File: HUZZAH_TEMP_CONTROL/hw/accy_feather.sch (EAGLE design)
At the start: 7 parts

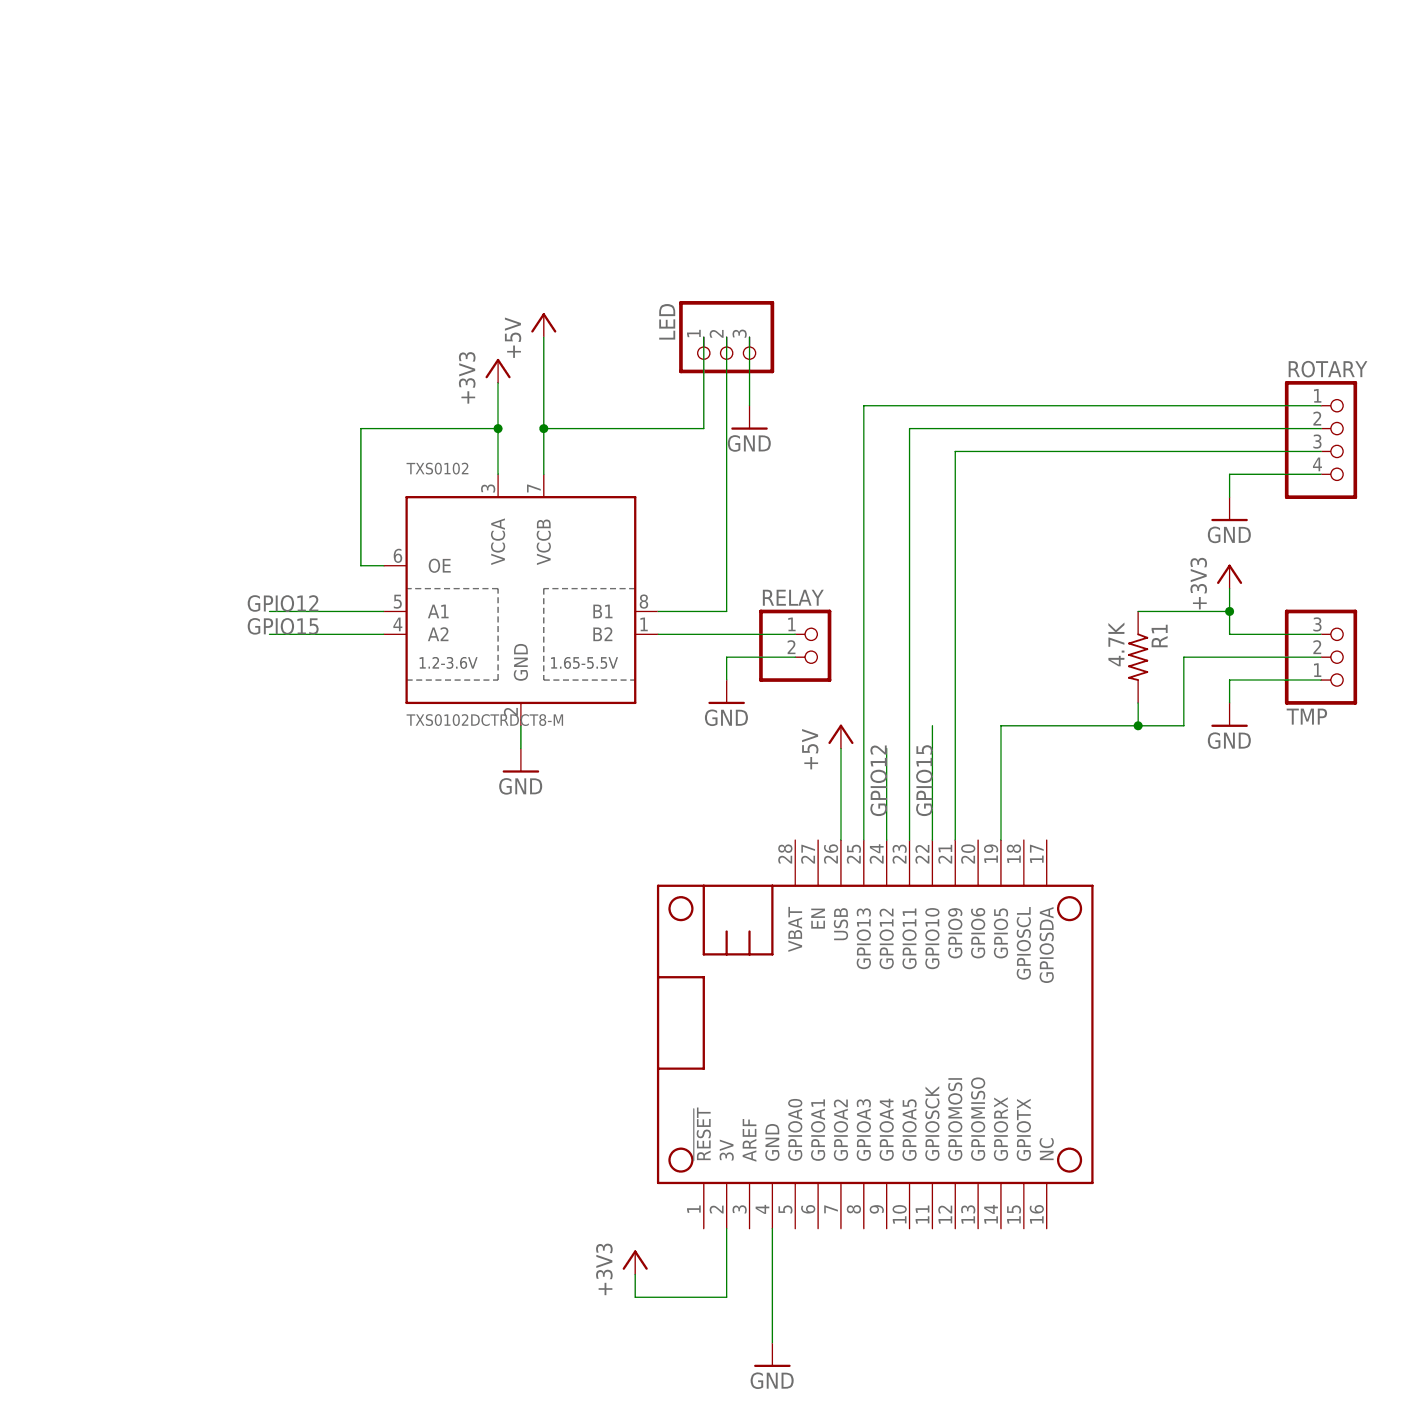
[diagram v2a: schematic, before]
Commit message: Accessory board version 2.0
Added a pulldown on the high voltage side of the relay output.  This
is needed because the level shifter can drive it high when it's floating
which causes board instability.

Added on-board 10A relay (Digi-Key Part #Z2763-ND) to the bottom side.
There are 2 choices for relay control now:
  - You can place the "Relay Drive" header and wire an external relay
    or SSR.  This is a good choice for high current loads like compressors.
                                   or
  - You can place the 10 relay Digi-Key Part #Z2763-ND) and the
    "Relay Switch" header.  The externally switched power can be run
    through the "Relay Switch" header.  This is good for lower current
    resistive heaters.
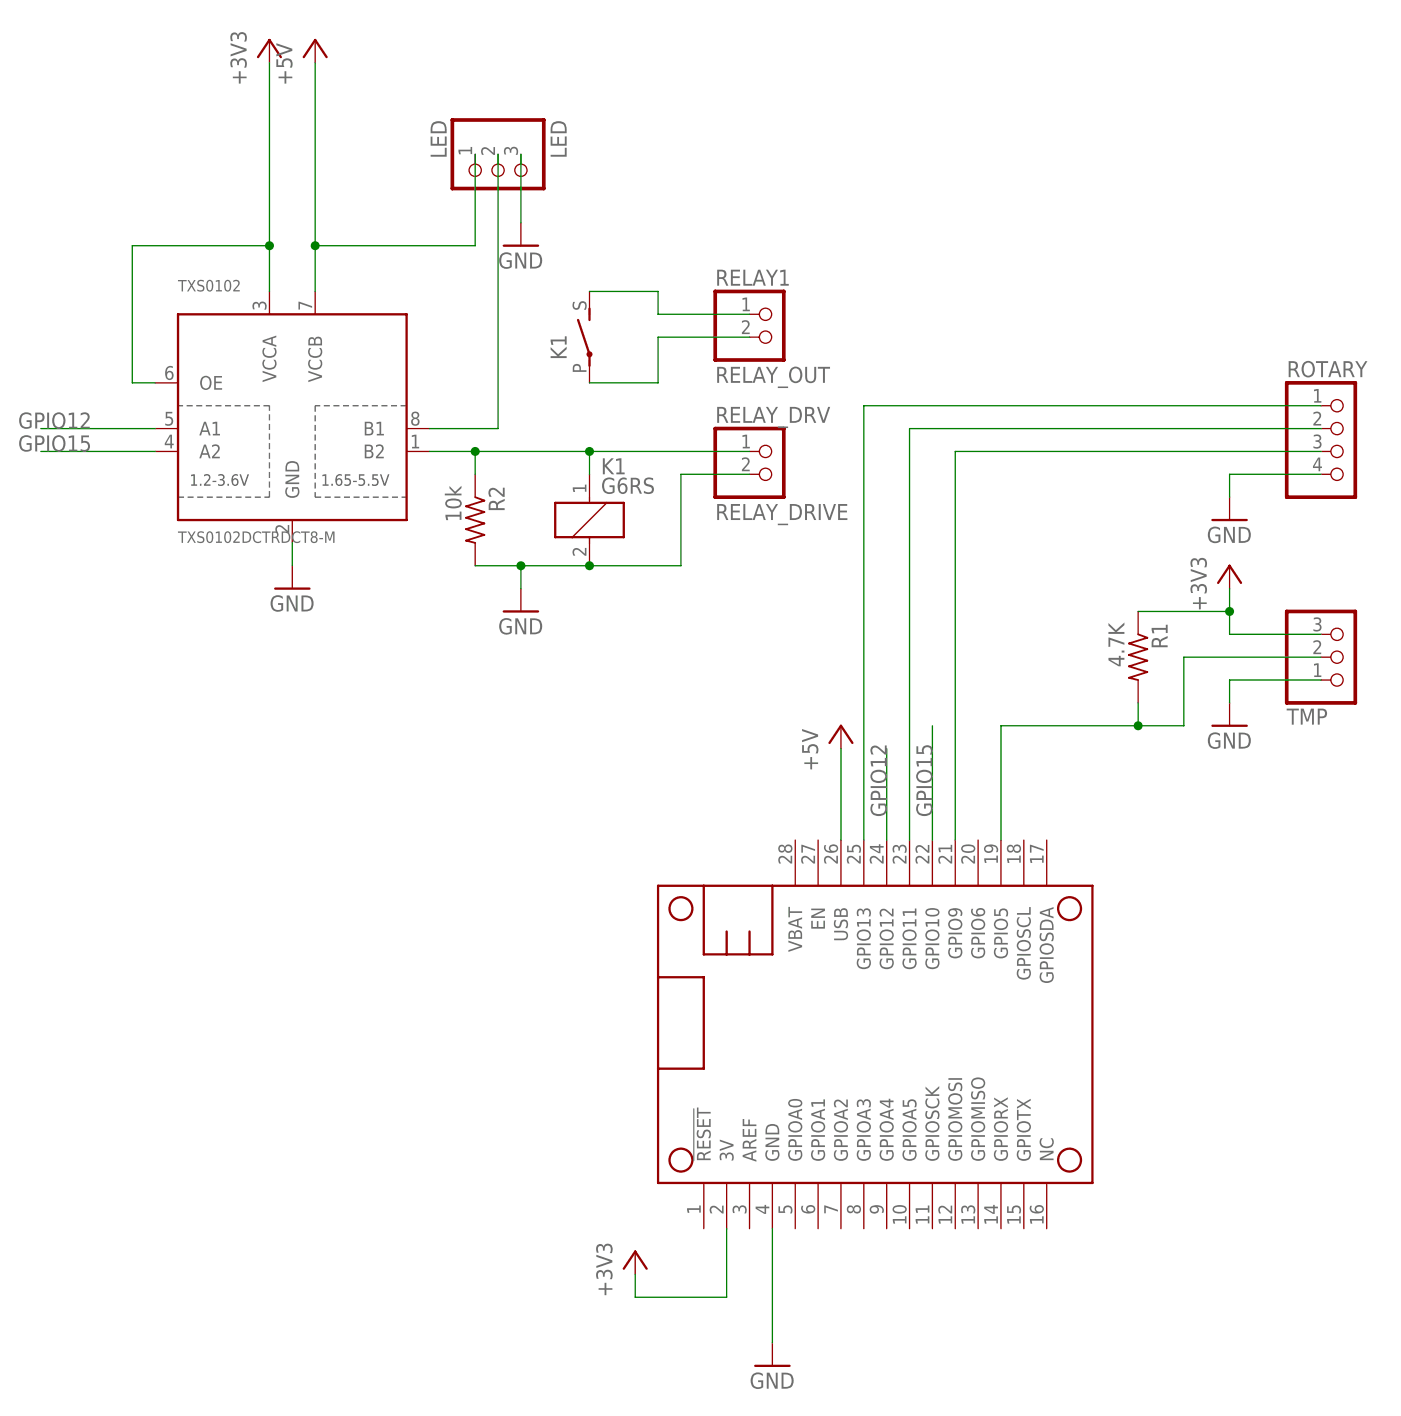
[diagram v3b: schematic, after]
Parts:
- removed RELAY: (no value), pinhead:PINHD-1X2
- added K1: G6RS, relay:G6RS
- added R2: 10k, resistor:R-US_R0603
- added RELAY1: RELAY_OUT, pinhead:PINHD-1X2
- added RELAY_DRV: RELAY_DRIVE, pinhead:PINHD-1X2
- LED: value (none) -> LED
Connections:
- new net N$2: K12.P, RELAY1.2
- new net RELAY_CTRL: K12.S, RELAY1.1
- net GND: now also K11.2, R2.2, RELAY_DRV.2; no longer RELAY.2
- net RELAY: now also K11.1, R2.1, RELAY_DRV.1; no longer RELAY.1
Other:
- moved on the sheet: LED, TXS0102
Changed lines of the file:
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@@
 <part name="GND5" library="supply1" deviceset="GND" device=""/>
 <part name="TMP" library="adafruit" deviceset="PINHD-1X3" device="CB"/>
-<part name="LED" library="adafruit" deviceset="PINHD-1X3" device="CB"/>
+<part name="LED" library="adafruit" deviceset="PINHD-1X3" device="CB" value="LED"/>
 <part name="GND6" library="supply1" deviceset="GND" device=""/>
 <part name="GND3" library="supply1" deviceset="GND" device=""/>
-<part name="RELAY" library="pinhead" deviceset="PINHD-1X2" device=""/>
+<part name="RELAY_DRV" library="pinhead" deviceset="PINHD-1X2" device="" value="RELAY_DRIVE"/>
 <part name="ROTARY" library="pinhead" deviceset="PINHD-1X4" device=""/>
 <part name="TXS0102" library="DZ" deviceset="TXS0102DCTR" device="DCT8-M"/>
+<part name="R2" library="resistor" deviceset="R-US_" device="R0603" value="10k"/>
+<part name="K1" library="relay" deviceset="G6RS" device=""/>
+<part name="RELAY1" library="pinhead" deviceset="PINHD-1X2" device="" value="RELAY_OUT"/>
 </parts>
 <sheets>
@@
 <instance part="P+1" gate="1" x="96.52" y="96.52"/>
 <instance part="+3V2" gate="G$1" x="139.7" y="114.3"/>
-<instance part="P+2" gate="1" x="63.5" y="142.24"/>
-<instance part="GND4" gate="1" x="60.96" y="91.44"/>
+<instance part="P+2" gate="1" x="38.1" y="172.72"/>
+<instance part="GND4" gate="1" x="35.56" y="111.76"/>
 <instance part="FRAME1" gate="G$1" x="0" y="0"/>
 <instance part="FRAME1" gate="G$2" x="147.32" y="0"/>
 <instance part="R1" gate="G$1" x="129.54" y="104.14" rot="R270"/>
-<instance part="+3V3" gate="G$1" x="58.42" y="137.16"/>
-<instance part="GND5" gate="1" x="86.36" y="129.54"/>
+<instance part="+3V3" gate="G$1" x="33.02" y="172.72"/>
+<instance part="GND5" gate="1" x="60.96" y="149.86"/>
 <instance part="TMP" gate="A" x="152.4" y="104.14" rot="MR180"/>
-<instance part="LED" gate="A" x="83.82" y="137.16" rot="MR270"/>
+<instance part="LED" gate="A" x="58.42" y="157.48" rot="MR270"/>
 <instance part="GND6" gate="1" x="139.7" y="119.38"/>
-<instance part="GND3" gate="1" x="83.82" y="99.06"/>
-<instance part="RELAY" gate="G$1" x="93.98" y="104.14"/>
+<instance part="GND3" gate="1" x="60.96" y="109.22"/>
+<instance part="RELAY_DRV" gate="G$1" x="88.9" y="124.46"/>
 <instance part="ROTARY" gate="A" x="152.4" y="127"/>
-<instance part="TXS0102" gate="A" x="48.26" y="99.06"/>
+<instance part="TXS0102" gate="A" x="22.86" y="119.38"/>
+<instance part="R2" gate="G$1" x="55.88" y="119.38" rot="R270"/>
+<instance part="K1" gate="1" x="68.58" y="119.38"/>
+<instance part="K1" gate="2" x="68.58" y="139.7"/>
+<instance part="RELAY1" gate="G$1" x="88.9" y="139.7"/>
 </instances>
 <busses>
@@
 <segment>
 <pinref part="GND4" gate="1" pin="GND"/>
-<wire x1="60.96" y1="93.98" x2="60.96" y2="96.52" width="0.1524" layer="91"/>
+<wire x1="35.56" y1="114.3" x2="35.56" y2="116.84" width="0.1524" layer="91"/>
 <pinref part="TXS0102" gate="A" pin="GND"/>
 </segment>
@@
 <pinref part="LED" gate="A" pin="3"/>
 <pinref part="GND5" gate="1" pin="GND"/>
-<wire x1="86.36" y1="139.7" x2="86.36" y2="132.08" width="0.1524" layer="91"/>
+<wire x1="60.96" y1="160.02" x2="60.96" y2="152.4" width="0.1524" layer="91"/>
 </segment>
 <segment>
 <pinref part="GND3" gate="1" pin="GND"/>
-<wire x1="83.82" y1="104.14" x2="83.82" y2="101.6" width="0.1524" layer="91"/>
-<pinref part="RELAY" gate="G$1" pin="2"/>
-<wire x1="91.44" y1="104.14" x2="83.82" y2="104.14" width="0.1524" layer="91"/>
+<wire x1="60.96" y1="114.3" x2="60.96" y2="111.76" width="0.1524" layer="91"/>
+<pinref part="R2" gate="G$1" pin="2"/>
+<wire x1="55.88" y1="114.3" x2="60.96" y2="114.3" width="0.1524" layer="91"/>
+<pinref part="RELAY_DRV" gate="G$1" pin="2"/>
+<wire x1="86.36" y1="124.46" x2="78.74" y2="124.46" width="0.1524" layer="91"/>
+<wire x1="78.74" y1="124.46" x2="78.74" y2="114.3" width="0.1524" layer="91"/>
+<wire x1="78.74" y1="114.3" x2="68.58" y2="114.3" width="0.1524" layer="91"/>
+<pinref part="K1" gate="1" pin="2"/>
+<wire x1="68.58" y1="114.3" x2="60.96" y2="114.3" width="0.1524" layer="91"/>
+<junction x="68.58" y="114.3"/>
+<junction x="60.96" y="114.3"/>
 </segment>
 </net>
@@
 <segment>
 <pinref part="P+2" gate="1" pin="+5V"/>
-<wire x1="63.5" y1="124.46" x2="63.5" y2="129.54" width="0.1524" layer="91"/>
+<wire x1="38.1" y1="144.78" x2="38.1" y2="149.86" width="0.1524" layer="91"/>
 <pinref part="LED" gate="A" pin="1"/>
-<wire x1="63.5" y1="129.54" x2="63.5" y2="139.7" width="0.1524" layer="91"/>
-<wire x1="81.28" y1="139.7" x2="81.28" y2="129.54" width="0.1524" layer="91"/>
-<wire x1="81.28" y1="129.54" x2="63.5" y2="129.54" width="0.1524" layer="91"/>
-<junction x="63.5" y="129.54"/>
+<wire x1="38.1" y1="149.86" x2="38.1" y2="170.18" width="0.1524" layer="91"/>
+<wire x1="55.88" y1="160.02" x2="55.88" y2="149.86" width="0.1524" layer="91"/>
+<wire x1="55.88" y1="149.86" x2="38.1" y2="149.86" width="0.1524" layer="91"/>
+<junction x="38.1" y="149.86"/>
 <pinref part="TXS0102" gate="A" pin="VCCB"/>
 </segment>
@@
 <net name="GPIO15" class="0">
 <segment>
-<wire x1="45.72" y1="106.68" x2="33.02" y2="106.68" width="0.1524" layer="91"/>
-<label x="30.48" y="106.68" size="1.778" layer="95"/>
+<wire x1="20.32" y1="127" x2="7.62" y2="127" width="0.1524" layer="91"/>
+<label x="5.08" y="127" size="1.778" layer="95"/>
 <pinref part="TXS0102" gate="A" pin="A2"/>
 </segment>
@@
 <segment>
 <pinref part="+3V3" gate="G$1" pin="+3V3"/>
-<wire x1="58.42" y1="124.46" x2="58.42" y2="129.54" width="0.1524" layer="91"/>
-<wire x1="58.42" y1="129.54" x2="58.42" y2="134.62" width="0.1524" layer="91"/>
-<wire x1="45.72" y1="114.3" x2="43.18" y2="114.3" width="0.1524" layer="91"/>
-<wire x1="43.18" y1="114.3" x2="43.18" y2="129.54" width="0.1524" layer="91"/>
-<wire x1="43.18" y1="129.54" x2="58.42" y2="129.54" width="0.1524" layer="91"/>
-<junction x="58.42" y="129.54"/>
+<wire x1="33.02" y1="144.78" x2="33.02" y2="149.86" width="0.1524" layer="91"/>
+<wire x1="33.02" y1="149.86" x2="33.02" y2="170.18" width="0.1524" layer="91"/>
+<wire x1="20.32" y1="134.62" x2="17.78" y2="134.62" width="0.1524" layer="91"/>
+<wire x1="17.78" y1="134.62" x2="17.78" y2="149.86" width="0.1524" layer="91"/>
+<junction x="33.02" y="149.86"/>
 <pinref part="TXS0102" gate="A" pin="VCCA"/>
 <pinref part="TXS0102" gate="A" pin="OE"/>
+<wire x1="17.78" y1="149.86" x2="33.02" y2="149.86" width="0.1524" layer="91"/>
 </segment>
 <segment>
@@
 <net name="LED_DATA" class="0">
 <segment>
-<wire x1="76.2" y1="109.22" x2="83.82" y2="109.22" width="0.1524" layer="91"/>
-<wire x1="83.82" y1="109.22" x2="83.82" y2="139.7" width="0.1524" layer="91"/>
+<wire x1="50.8" y1="129.54" x2="58.42" y2="129.54" width="0.1524" layer="91"/>
+<wire x1="58.42" y1="129.54" x2="58.42" y2="160.02" width="0.1524" layer="91"/>
 <pinref part="LED" gate="A" pin="2"/>
 <pinref part="TXS0102" gate="A" pin="B1"/>
@@
 <net name="GPIO12" class="0">
 <segment>
-<wire x1="45.72" y1="109.22" x2="33.02" y2="109.22" width="0.1524" layer="91"/>
-<label x="30.48" y="109.22" size="1.778" layer="95"/>
+<wire x1="20.32" y1="129.54" x2="7.62" y2="129.54" width="0.1524" layer="91"/>
+<label x="5.08" y="129.54" size="1.778" layer="95"/>
 <pinref part="TXS0102" gate="A" pin="A1"/>
 </segment>
@@
 <net name="RELAY" class="0">
 <segment>
-<pinref part="RELAY" gate="G$1" pin="1"/>
-<wire x1="91.44" y1="106.68" x2="76.2" y2="106.68" width="0.1524" layer="91"/>
+<pinref part="RELAY_DRV" gate="G$1" pin="1"/>
+<wire x1="86.36" y1="127" x2="68.58" y2="127" width="0.1524" layer="91"/>
 <pinref part="TXS0102" gate="A" pin="B2"/>
-</segment>
-</net>
+<pinref part="R2" gate="G$1" pin="1"/>
+<wire x1="68.58" y1="127" x2="55.88" y2="127" width="0.1524" layer="91"/>
+<wire x1="55.88" y1="127" x2="50.8" y2="127" width="0.1524" layer="91"/>
+<wire x1="55.88" y1="124.46" x2="55.88" y2="127" width="0.1524" layer="91"/>
+<junction x="55.88" y="127"/>
+<pinref part="K1" gate="1" pin="1"/>
+<wire x1="68.58" y1="124.46" x2="68.58" y2="127" width="0.1524" layer="91"/>
+<junction x="68.58" y="127"/>
+</segment>
+</net>
+<net name="N$2" class="0">
+<segment>
+<pinref part="RELAY1" gate="G$1" pin="2"/>
+<wire x1="86.36" y1="139.7" x2="76.2" y2="139.7" width="0.1524" layer="91"/>
+<wire x1="76.2" y1="139.7" x2="76.2" y2="134.62" width="0.1524" layer="91"/>
+<pinref part="K1" gate="2" pin="P"/>
+<wire x1="76.2" y1="134.62" x2="68.58" y2="134.62" width="0.1524" layer="91"/>
+</segment>
+</net>
+<net name="RELAY_CTRL" class="0">
+<segment>
+<pinref part="RELAY1" gate="G$1" pin="1"/>
+<wire x1="86.36" y1="142.24" x2="76.2" y2="142.24" width="0.1524" layer="91"/>
+<wire x1="76.2" y1="142.24" x2="76.2" y2="144.78" width="0.1524" layer="91"/>
+<pinref part="K1" gate="2" pin="S"/>
+<wire x1="76.2" y1="144.78" x2="68.58" y2="144.78" width="0.1524" layer="91"/>
+</segment>
+</net>
